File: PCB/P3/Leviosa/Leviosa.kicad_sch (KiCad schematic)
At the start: 57 parts, among them J1 Barrel_Jack, J2 2.54mm 1x03 Spare, U1 MX27517, U2 MCP6001R

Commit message: create PCB initial draft
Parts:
- removed R16: 3.9kΩ, Resistor_SMD:R_0603_1608Metric, symbol Device:R_US
- Coil1: footprint Inductor_THT:L_Axial_L5.0mm_D3.6mm_P10.00mm_Horizontal_Murata_BL01RN1A2A2 -> Connector_PinHeader_2.54mm:PinHeader_2x01_P2.54mm_Vertical
- R5, R8: footprint Resistor_SMD:R_1206_3216Metric -> Resistor_SMD:R_0805_2012Metric_Pad1.20x1.40mm_HandSolder
- TP_12V1, TP_Fault1, TP_GND1, TP_Vout1, TP_coilOut1, TP_setPt1: footprint TestPoint:TestPoint_Pad_D1.5mm -> TestPoint:TestPoint_Pad_D1.0mm
- renumbered C_coil2 to C_hall1, U1 to gate_driver1, hall_sensor1 to hall1, U2 to opAmp1
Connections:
- no-connect marks 0 -> 1
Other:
- note added: "Pulled high by default."
- note removed: "can leave floating. Auto pulled high"
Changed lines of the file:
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@@
 		)
 	)
-	(text "can leave floating. Auto pulled high"
+	(text "Pulled high by default."
 		(exclude_from_sim no)
-		(at 275.59 105.664 0)
+		(at 262.89 105.664 0)
 		(effects
 			(font
@@
 	(text "RC filter:\nFc = 1/ (2pi * R * C)\nlet R = 8.2Ω and C = 4.7nF\nFc = 4.1MHz"
 		(exclude_from_sim no)
-		(at 172.72 148.336 0)
+		(at 176.53 148.59 0)
 		(effects
 			(font
@@
 	)
 	(junction
-		(at 185.42 149.86)
-		(diameter 0)
-		(color 0 0 0 0)
-	)
-	(junction
 		(at 91.44 38.1)
 		(diameter 0)
@@
 		(color 0 0 0 0)
 	)
+	(no_connect
+		(at 238.76 105.41)
+	)
 	(wire
 		(pts
@@
 	(wire
 		(pts
-			(xy 205.74 149.86) (xy 205.74 100.33)
+			(xy 205.74 143.51) (xy 205.74 100.33)
 		)
 		(stroke
@@
 	(wire
 		(pts
-			(xy 185.42 149.86) (xy 205.74 149.86)
+			(xy 185.42 143.51) (xy 205.74 143.51)
 		)
 		(stroke
@@
 	(wire
 		(pts
-			(xy 151.13 142.24) (xy 151.13 124.46)
-		)
-		(stroke
-			(width 0)
-			(type default)
-		)
-	)
-	(wire
-		(pts
 			(xy 102.87 38.1) (xy 96.52 38.1)
 		)
@@
 	(wire
 		(pts
-			(xy 185.42 143.51) (xy 185.42 149.86)
+			(xy 151.13 124.46) (xy 151.13 142.24)
 		)
 		(stroke
@@
 	)
 	(label "instrumental_out"
-		(at 151.13 124.46 0)
+		(at 151.13 129.54 0)
 		(effects
 			(font
@@
 	)
 	(label "5V"
-		(at 177.8 149.86 180)
-		(effects
-			(font
-				(size 1.27 1.27)
-			)
-			(justify right bottom)
-		)
-	)
-	(label "5V"
 		(at 140.97 114.3 0)
 		(effects
@@
 	)
 	(symbol
-		(lib_id "Device:R_US")
-		(at 181.61 149.86 270)
-		(unit 1)
-		(exclude_from_sim no)
-		(in_bom yes)
-		(on_board yes)
-		(dnp no)
-		(property "Reference" "R16"
-			(at 181.356 145.288 90)
-			(effects
-				(font
-					(size 1.27 1.27)
-				)
-			)
-		)
-		(property "Value" "3.9kΩ"
-			(at 181.61 147.32 90)
-			(effects
-				(font
-					(size 1.27 1.27)
-				)
-			)
-		)
-		(property "Footprint" "Resistor_SMD:R_0603_1608Metric"
-			(at 181.356 150.876 90)
-			(effects
-				(font
-					(size 1.27 1.27)
-				)
-				(hide yes)
-			)
-		)
-		(property "Datasheet" "~"
-			(at 181.61 149.86 0)
-			(effects
-				(font
-					(size 1.27 1.27)
-				)
-				(hide yes)
-			)
-		)
-		(property "Description" ""
-			(at 181.61 149.86 0)
-			(effects
-				(font
-					(size 1.27 1.27)
-				)
-			)
-		)
-		(property "Link" "https://jlcpcb.com/partdetail/23745-0603WAF3901T5E/C23018"
-			(at 181.61 149.86 90)
-			(effects
-				(font
-					(size 1.27 1.27)
-				)
-				(hide yes)
-			)
-		)
-		(pin "1"
-		)
-		(pin "2"
-		)
-		(instances
-			(project "Leviosa"
-				(path "/fe766911-203b-467c-b704-d4bd488f6c98"
-					(reference "R16")
-					(unit 1)
-				)
-			)
-		)
-	)
-	(symbol
 		(lib_id "Device:C")
 		(at 182.88 46.99 0)
@@
 			)
 		)
-		(property "Footprint" "Resistor_SMD:R_1206_3216Metric"
+		(property "Footprint" "Resistor_SMD:R_0805_2012Metric_Pad1.20x1.40mm_HandSolder"
 			(at 209.804 99.314 90)
 			(effects
@@
 			)
 		)
-		(property "Footprint" "TestPoint:TestPoint_Pad_D1.5mm"
+		(property "Footprint" "TestPoint:TestPoint_Pad_D1.0mm"
 			(at 30.48 184.15 0)
 			(effects
@@
 		(on_board yes)
 		(dnp no)
-		(property "Reference" "U2"
+		(property "Reference" "opAmp1"
 			(at 147.574 115.062 0)
 			(effects
@@
 			(project ""
 				(path "/fe766911-203b-467c-b704-d4bd488f6c98"
-					(reference "U2")
+					(reference "opAmp1")
 					(unit 1)
 				)
@@
 			)
 		)
-		(property "Footprint" "Inductor_THT:L_Axial_L5.0mm_D3.6mm_P10.00mm_Horizontal_Murata_BL01RN1A2A2"
+		(property "Footprint" "Connector_PinHeader_2.54mm:PinHeader_2x01_P2.54mm_Vertical"
 			(at 207.01 46.99 0)
 			(effects
@@
 			)
 		)
-		(property "Footprint" "TestPoint:TestPoint_Pad_D1.5mm"
+		(property "Footprint" "TestPoint:TestPoint_Pad_D1.0mm"
 			(at 254 97.79 0)
 			(effects
@@
 		(on_board yes)
 		(dnp no)
-		(property "Reference" "hall_sensor1"
+		(property "Reference" "hall1"
 			(at 136.398 110.49 0)
 			(effects
@@
 			(project "Leviosa"
 				(path "/fe766911-203b-467c-b704-d4bd488f6c98"
-					(reference "hall_sensor1")
+					(reference "hall1")
 					(unit 1)
 				)
@@
 		(on_board yes)
 		(dnp no)
-		(property "Reference" "U1"
+		(property "Reference" "gate_driver1"
 			(at 228.092 110.744 0)
 			(effects
@@
 			)
 		)
-		(property "Datasheet" "https://jlcpcb.com/api/file/downloadByFileSystemAccessId/8601069044485406720"
+		(property "Datasheet" "https://jlcpcb.com/api/file/downloadByFileSystemAccessId/8603011825076084736"
 			(at 217.17 96.52 0)
 			(effects
@@
 			(project ""
 				(path "/fe766911-203b-467c-b704-d4bd488f6c98"
-					(reference "U1")
+					(reference "gate_driver1")
 					(unit 1)
 				)
@@
 			)
 		)
-		(property "Footprint" "TestPoint:TestPoint_Pad_D1.5mm"
+		(property "Footprint" "TestPoint:TestPoint_Pad_D1.0mm"
 			(at 62.23 59.69 0)
 			(effects
@@
 			)
 		)
-		(property "Footprint" "TestPoint:TestPoint_Pad_D1.5mm"
+		(property "Footprint" "TestPoint:TestPoint_Pad_D1.0mm"
 			(at 92.71 67.31 0)
 			(effects
@@
 			)
 		)
-		(property "Footprint" "TestPoint:TestPoint_Pad_D1.5mm"
+		(property "Footprint" "TestPoint:TestPoint_Pad_D1.0mm"
 			(at 201.93 83.82 0)
 			(effects
@@
 		(on_board yes)
 		(dnp no)
-		(property "Reference" "C_coil2"
+		(property "Reference" "C_hall1"
 			(at 167.386 135.128 0)
 			(effects
@@
 			(project "Leviosa"
 				(path "/fe766911-203b-467c-b704-d4bd488f6c98"
-					(reference "C_coil2")
+					(reference "C_hall1")
 					(unit 1)
 				)
@@
 			)
 		)
-		(property "Footprint" "TestPoint:TestPoint_Pad_D1.5mm"
+		(property "Footprint" "TestPoint:TestPoint_Pad_D1.0mm"
 			(at 30.48 162.56 0)
 			(effects
@@
 			)
 		)
-		(property "Footprint" "Resistor_SMD:R_1206_3216Metric"
+		(property "Footprint" "Resistor_SMD:R_0805_2012Metric_Pad1.20x1.40mm_HandSolder"
 			(at 239.014 96.266 90)
 			(effects

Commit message: update PCB and schematic slightly
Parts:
- removed H3: MountingHole, MountingHole:MountingHole_3.2mm_M3_ISO7380, symbol Mechanical:MountingHole
- V_reg1: Link (none) -> https://jlcpcb.com/partdetail/onsemi-MC7805BD2TR4G/C15833
- renumbered TP_12V1 to 12V1, TP_5V1 to 5V1, Cbypass2 to C_MCU1, Cbypass1 to C_sense1, TP_GND1 to GND1, Q_setPt1 to Q1, Servo1 to Srvo1, Servo2 to Srvo2, current_lim1 to U_Ilim1, current_sense1 to U_sense1, TP_Vout1 to Vout1, comparator1 to cmprtr1, TP_coilOut1 to coilOut1, TP_Fault1 to fault1, gate_driver1 to gtDrvr1, TP_setPt1 to gtOut1, Pot_setPt1 to pot1
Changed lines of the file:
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@@
 		(on_board yes)
 		(dnp no)
-		(property "Reference" "Cbypass1"
+		(property "Reference" "C_sense1"
 			(at 254.508 46.736 90)
 			(effects
@@
 			(project "Leviosa"
 				(path "/fe766911-203b-467c-b704-d4bd488f6c98"
-					(reference "Cbypass1")
+					(reference "C_sense1")
 					(unit 1)
 				)
@@
 		(on_board yes)
 		(dnp no)
-		(property "Reference" "current_sense1"
+		(property "Reference" "U_sense1"
 			(at 256.286 65.278 0)
 			(effects
@@
 			(project ""
 				(path "/fe766911-203b-467c-b704-d4bd488f6c98"
-					(reference "current_sense1")
+					(reference "U_sense1")
 					(unit 1)
 				)
@@
 		(dnp no)
 		(fields_autoplaced yes)
-		(property "Reference" "Cbypass2"
+		(property "Reference" "C_MCU1"
 			(at 73.66 144.7799 0)
 			(effects
@@
 			(project "Leviosa"
 				(path "/fe766911-203b-467c-b704-d4bd488f6c98"
-					(reference "Cbypass2")
+					(reference "C_MCU1")
 					(unit 1)
 				)
@@
 		(on_board yes)
 		(dnp no)
-		(property "Reference" "TP_5V1"
+		(property "Reference" "5V1"
 			(at 93.98 26.67 0)
 			(effects
@@
 			(project "Leviosa"
 				(path "/fe766911-203b-467c-b704-d4bd488f6c98"
-					(reference "TP_5V1")
+					(reference "5V1")
 					(unit 1)
 				)
@@
 		(on_board yes)
 		(dnp no)
-		(property "Reference" "Servo2"
+		(property "Reference" "Srvo2"
 			(at 97.028 140.208 90)
 			(effects
@@
 			(project "Leviosa"
 				(path "/fe766911-203b-467c-b704-d4bd488f6c98"
-					(reference "Servo2")
+					(reference "Srvo2")
 					(unit 1)
 				)
@@
 		(on_board yes)
 		(dnp no)
-		(property "Reference" "current_lim1"
+		(property "Reference" "U_Ilim1"
 			(at 43.18 41.91 0)
 			(effects
@@
 			(project "Leviosa"
 				(path "/fe766911-203b-467c-b704-d4bd488f6c98"
-					(reference "current_lim1")
+					(reference "U_Ilim1")
 					(unit 1)
 				)
@@
 		(dnp no)
 		(fields_autoplaced yes)
-		(property "Reference" "TP_GND1"
+		(property "Reference" "GND1"
 			(at 35.56 177.7999 90)
 			(effects
@@
 			(project "Leviosa"
 				(path "/fe766911-203b-467c-b704-d4bd488f6c98"
-					(reference "TP_GND1")
+					(reference "GND1")
 					(unit 1)
 				)
@@
 		(on_board yes)
 		(dnp no)
-		(property "Reference" "Q_setPt1"
+		(property "Reference" "Q1"
 			(at 236.474 75.946 90)
 			(effects
@@
 			(project ""
 				(path "/fe766911-203b-467c-b704-d4bd488f6c98"
-					(reference "Q_setPt1")
+					(reference "Q1")
 					(unit 1)
 				)
@@
 			)
 		)
+		(property "Link" "https://jlcpcb.com/partdetail/onsemi-MC7805BD2TR4G/C15833"
+			(at 83.82 38.1 0)
+			(effects
+				(font
+					(size 1.27 1.27)
+				)
+				(hide yes)
+			)
+		)
 		(pin "2"
 		)
@@
 		(on_board yes)
 		(dnp no)
-		(property "Reference" "TP_setPt1"
+		(property "Reference" "gtOut1"
 			(at 271.272 92.964 90)
 			(effects
@@
 			(project "Leviosa"
 				(path "/fe766911-203b-467c-b704-d4bd488f6c98"
-					(reference "TP_setPt1")
+					(reference "gtOut1")
 					(unit 1)
 				)
@@
 		(on_board yes)
 		(dnp no)
-		(property "Reference" "gate_driver1"
+		(property "Reference" "gtDrvr1"
 			(at 228.092 110.744 0)
 			(effects
@@
 			(project ""
 				(path "/fe766911-203b-467c-b704-d4bd488f6c98"
-					(reference "gate_driver1")
+					(reference "gtDrvr1")
 					(unit 1)
 				)
@@
 		(on_board yes)
 		(dnp no)
-		(property "Reference" "TP_Fault1"
+		(property "Reference" "fault1"
 			(at 67.31 50.8 90)
 			(effects
@@
 			(project "Leviosa"
 				(path "/fe766911-203b-467c-b704-d4bd488f6c98"
-					(reference "TP_Fault1")
+					(reference "fault1")
 					(unit 1)
 				)
@@
 		(on_board yes)
 		(dnp no)
-		(property "Reference" "TP_Vout1"
-			(at 98.044 64.262 0)
+		(property "Reference" "Vout1"
+			(at 95.758 64.516 0)
 			(effects
 				(font
@@
 			(project "Leviosa"
 				(path "/fe766911-203b-467c-b704-d4bd488f6c98"
-					(reference "TP_Vout1")
+					(reference "Vout1")
 					(unit 1)
 				)
@@
 		(on_board yes)
 		(dnp no)
-		(property "Reference" "Servo1"
+		(property "Reference" "Srvo1"
 			(at 105.156 161.544 90)
 			(effects
@@
 			(project "Leviosa"
 				(path "/fe766911-203b-467c-b704-d4bd488f6c98"
-					(reference "Servo1")
+					(reference "Srvo1")
 					(unit 1)
 				)
@@
 		(on_board yes)
 		(dnp no)
-		(property "Reference" "Pot_setPt1"
+		(property "Reference" "pot1"
 			(at 141.732 48.26 0)
 			(effects
@@
 			(project "Leviosa"
 				(path "/fe766911-203b-467c-b704-d4bd488f6c98"
-					(reference "Pot_setPt1")
-					(unit 1)
-				)
-			)
-		)
-	)
-	(symbol
-		(lib_id "Mechanical:MountingHole")
-		(at 152.4 186.69 0)
-		(unit 1)
-		(exclude_from_sim no)
-		(in_bom no)
-		(on_board yes)
-		(dnp no)
-		(fields_autoplaced yes)
-		(property "Reference" "H3"
-			(at 154.94 185.4199 0)
-			(effects
-				(font
-					(size 1.27 1.27)
-				)
-				(justify left)
-			)
-		)
-		(property "Value" "MountingHole"
-			(at 154.94 187.9599 0)
-			(effects
-				(font
-					(size 1.27 1.27)
-				)
-				(justify left)
-			)
-		)
-		(property "Footprint" "MountingHole:MountingHole_3.2mm_M3_ISO7380"
-			(at 152.4 186.69 0)
-			(effects
-				(font
-					(size 1.27 1.27)
-				)
-				(hide yes)
-			)
-		)
-		(property "Datasheet" "~"
-			(at 152.4 186.69 0)
-			(effects
-				(font
-					(size 1.27 1.27)
-				)
-				(hide yes)
-			)
-		)
-		(property "Description" "Mounting Hole without connection"
-			(at 152.4 186.69 0)
-			(effects
-				(font
-					(size 1.27 1.27)
-				)
-				(hide yes)
-			)
-		)
-		(instances
-			(project "Leviosa"
-				(path "/fe766911-203b-467c-b704-d4bd488f6c98"
-					(reference "H3")
+					(reference "pot1")
 					(unit 1)
 				)
@@
 		(on_board yes)
 		(dnp no)
-		(property "Reference" "comparator1"
+		(property "Reference" "cmprtr1"
 			(at 188.722 138.938 90)
 			(effects
@@
 			(project ""
 				(path "/fe766911-203b-467c-b704-d4bd488f6c98"
-					(reference "comparator1")
+					(reference "cmprtr1")
 					(unit 2)
 				)
@@
 		(on_board yes)
 		(dnp no)
-		(property "Reference" "TP_coilOut1"
+		(property "Reference" "coilOut1"
 			(at 208.788 86.36 0)
 			(effects
@@
 			(project "Leviosa"
 				(path "/fe766911-203b-467c-b704-d4bd488f6c98"
-					(reference "TP_coilOut1")
+					(reference "coilOut1")
 					(unit 1)
 				)
@@
 		(dnp no)
 		(fields_autoplaced yes)
-		(property "Reference" "TP_12V1"
+		(property "Reference" "12V1"
 			(at 35.56 156.2099 90)
 			(effects
@@
 			(project "Leviosa"
 				(path "/fe766911-203b-467c-b704-d4bd488f6c98"
-					(reference "TP_12V1")
+					(reference "12V1")
 					(unit 1)
 				)
@@
 		(on_board yes)
 		(dnp no)
-		(property "Reference" "comparator1"
+		(property "Reference" "cmprtr1"
 			(at 168.148 110.744 0)
 			(effects
@@
 			(project ""
 				(path "/fe766911-203b-467c-b704-d4bd488f6c98"
-					(reference "comparator1")
+					(reference "cmprtr1")
 					(unit 3)
 				)
@@
 		(on_board yes)
 		(dnp no)
-		(property "Reference" "comparator1"
+		(property "Reference" "cmprtr1"
 			(at 189.23 111.252 90)
 			(effects
@@
 			(project ""
 				(path "/fe766911-203b-467c-b704-d4bd488f6c98"
-					(reference "comparator1")
+					(reference "cmprtr1")
 					(unit 1)
 				)

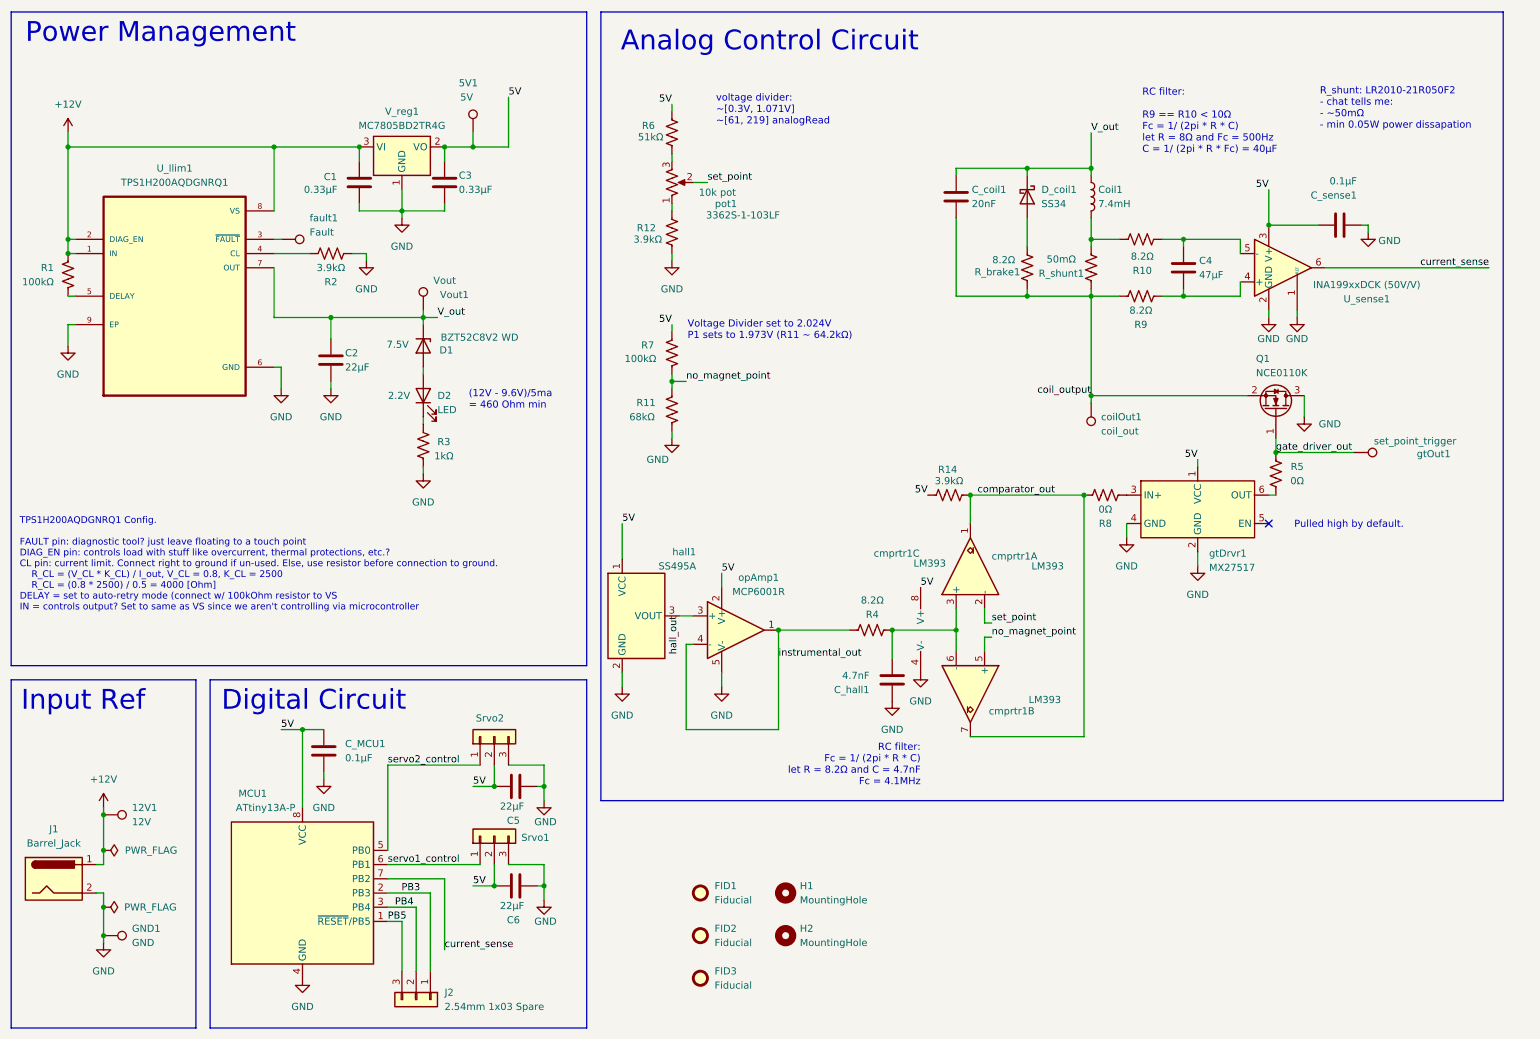
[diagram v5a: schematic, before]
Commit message: Update - Dec 9th
- Updated labels for power, components and TPs
- Changed standard comp to 0603 knowing we have these
- Updated TPS symbol
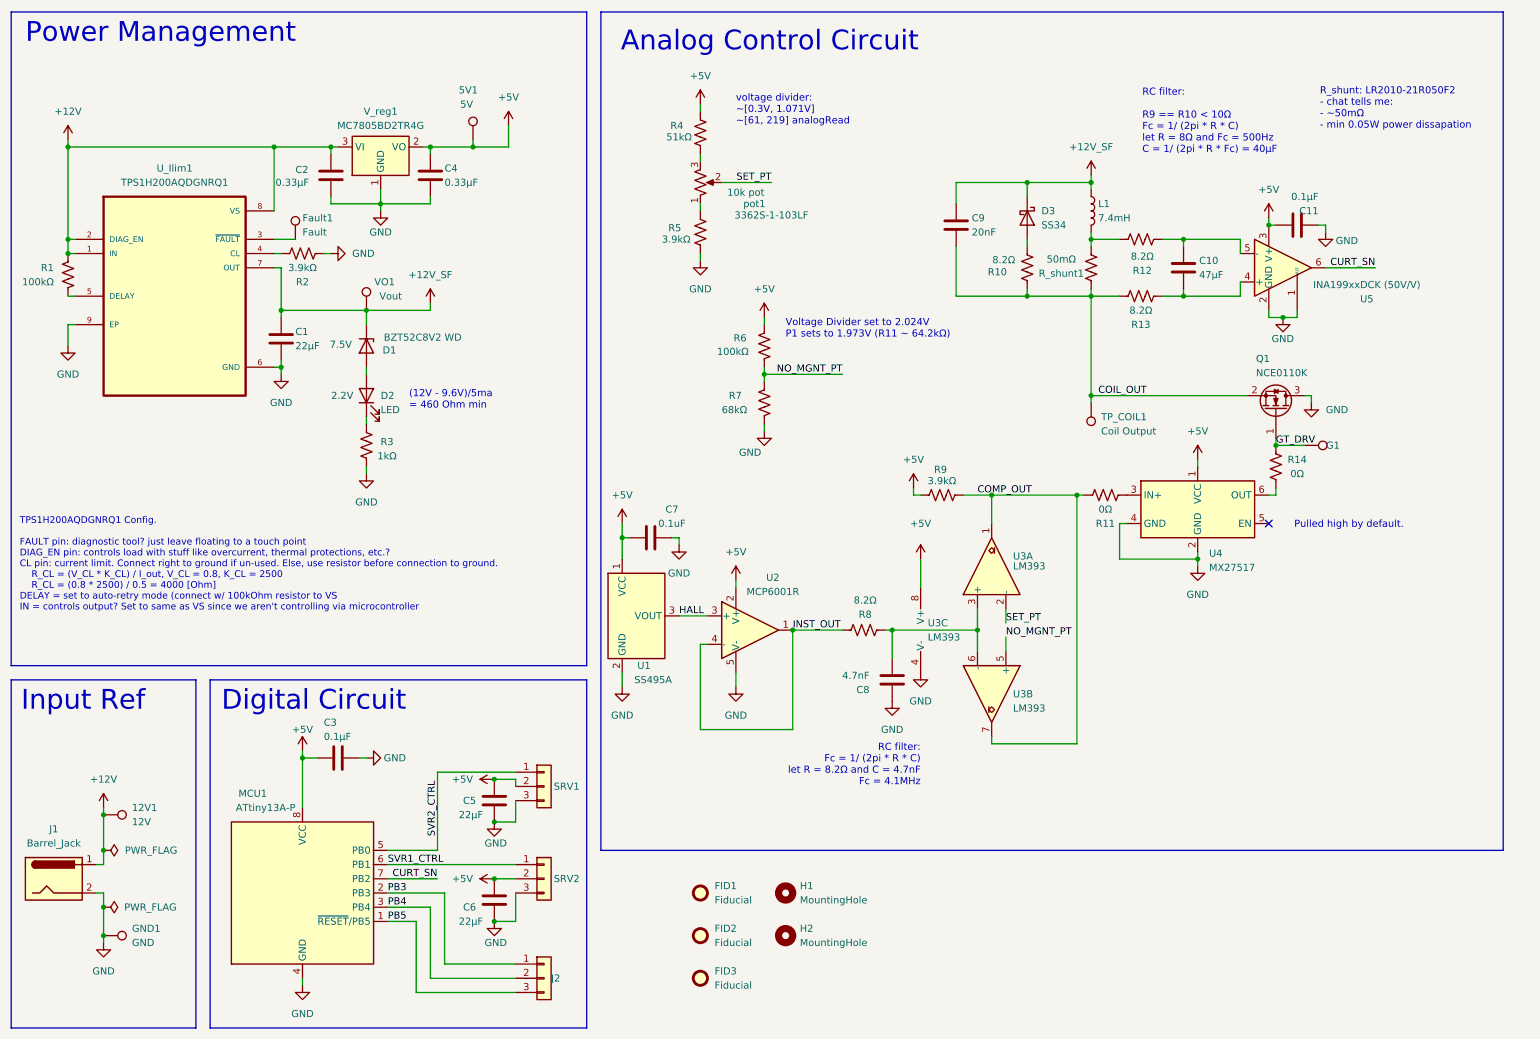
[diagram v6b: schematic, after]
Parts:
- added C7: 0.1uF, Capacitor_SMD:C_0603_1608Metric, symbol Device:C
- C11: renamed from C_sense1; footprint Capacitor_SMD:C_0402_1005Metric -> Capacitor_SMD:C_0603_1608Metric
- C3: renamed from C_MCU1; footprint Capacitor_SMD:C_0402_1005Metric -> Capacitor_SMD:C_0603_1608Metric
- R1, R3: footprint Resistor_SMD:R_0805_2012Metric_Pad1.20x1.40mm_HandSolder -> Resistor_SMD:R_0603_1608Metric
- R11: renamed from R8; footprint Resistor_SMD:R_0805_2012Metric_Pad1.20x1.40mm_HandSolder -> Resistor_SMD:R_0603_1608Metric
- R14: renamed from R5; footprint Resistor_SMD:R_0805_2012Metric_Pad1.20x1.40mm_HandSolder -> Resistor_SMD:R_0603_1608Metric
- R6: renamed from R7; footprint Resistor_SMD:R_0805_2012Metric_Pad1.20x1.40mm_HandSolder -> Resistor_SMD:R_0603_1608Metric
- TP_COIL1: renamed from coilOut1; value coil_out -> Coil Output
- U_Ilim1: MF Texas Instruments -> (none); MP TPS1H200AQDGNRQ1 -> (none); PACKAGE HVSSOP-8 Texas Instruments -> (none); PRICE None -> (none); PURCHASE-URL https://www.snapeda.com/api/url_track_click_mouser/?unipart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 -> (none); SNAPEDA_LINK https://www.snapeda.com/parts/TPS1H200AQDGNRQ1/Texas+Instru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 -> (none)
- renumbered C2 to C1, C4 to C10, C1 to C2, C3 to C4, C_hall1 to C8, C_coil1 to C9, D_coil1 to D3, fault1 to Fault1, gtOut1 to G1, Coil1 to L1, R_brake1 to R10, R10 to R12, R9 to R13, R6 to R4, R12 to R5, R11 to R7, R4 to R8, R14 to R9, Srvo2 to SRV1, Srvo1 to SRV2, hall1 to U1, opAmp1 to U2, cmprtr1 to U3, gtDrvr1 to U4, U_sense1 to U5, Vout1 to VO1
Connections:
- net GND: now also C7.2
- net 5V renamed +5V
- net +5V: now also C7.1
- net V_out renamed +12V_SF
- net coil_output renamed COIL_OUT
- net comparator_out renamed COMP_OUT
- net current_sense renamed CURT_SN
- net gate_driver_out renamed GT_DRV
- net hall_out renamed HALL
- net instrumental_out renamed INST_OUT
- net no_magnet_point renamed NO_MGNT_PT
- net servo1_control renamed SVR1_CTRL
- net servo2_control renamed SVR2_CTRL
- net set_point renamed SET_PT
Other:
- moved on the sheet: 5V1, C1, C11, C2, C3, C4, C5, C6, C9, D1, D2, D3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
